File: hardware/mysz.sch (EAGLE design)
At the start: 17 parts, among them IC1 LM1117T(H)-3.3, U1 NUCLEO-L053R8, X2 332-18

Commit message: Add Gyro schemat
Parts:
- removed U$2: DISPLAY-NOKIA-3310, diy-modules:DISPLAY-NOKIA-3310
- removed X2: 332-18, con-garry:332-18
- added GYRO: (no value), pinhead:PINHD-1X10
- added PCD8544: (no value), pinhead:PINHD-1X7/90
- added R3, R4: 22k, rcl:R-EU_0207/10
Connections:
- new net GYRO_CS: GYRO.3
- new net GYRO_DEN: GYRO.1
- new net GYRO_INT1: GYRO.2
- new net GYRO_SCL: GYRO.6, R3.1
- new net GYRO_SDA: GYRO.7, R4.1
- new net LCD_CE: PCD8544.2
- new net LCD_DC: PCD8544.3
- new net LCD_RST: PCD8544.1
- new net N$4: GYRO.10, GYRO.4
- net +3V3: now also R3.2, R4.2
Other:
- moved on the sheet: C1, C2, C3, C4, IC1, POWER

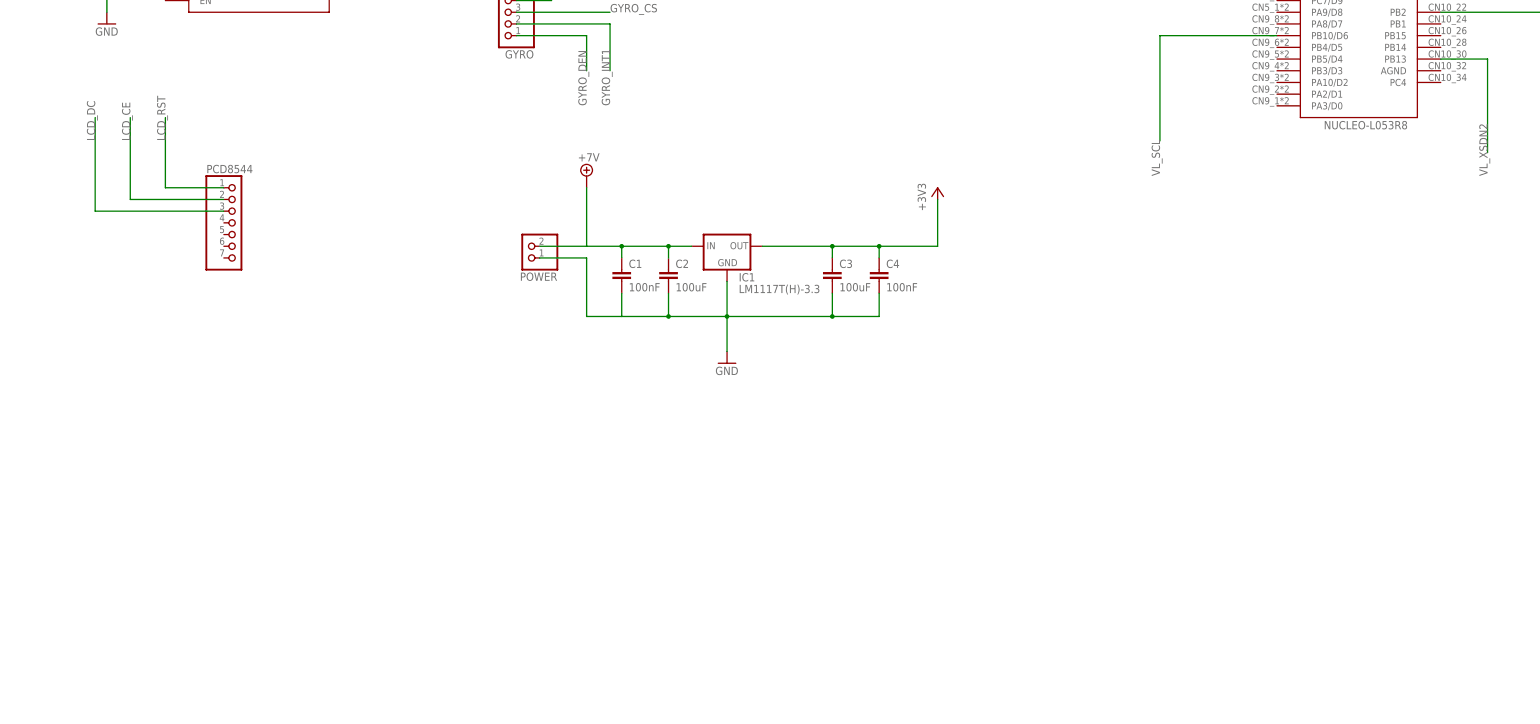
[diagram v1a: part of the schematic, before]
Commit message: Add driver
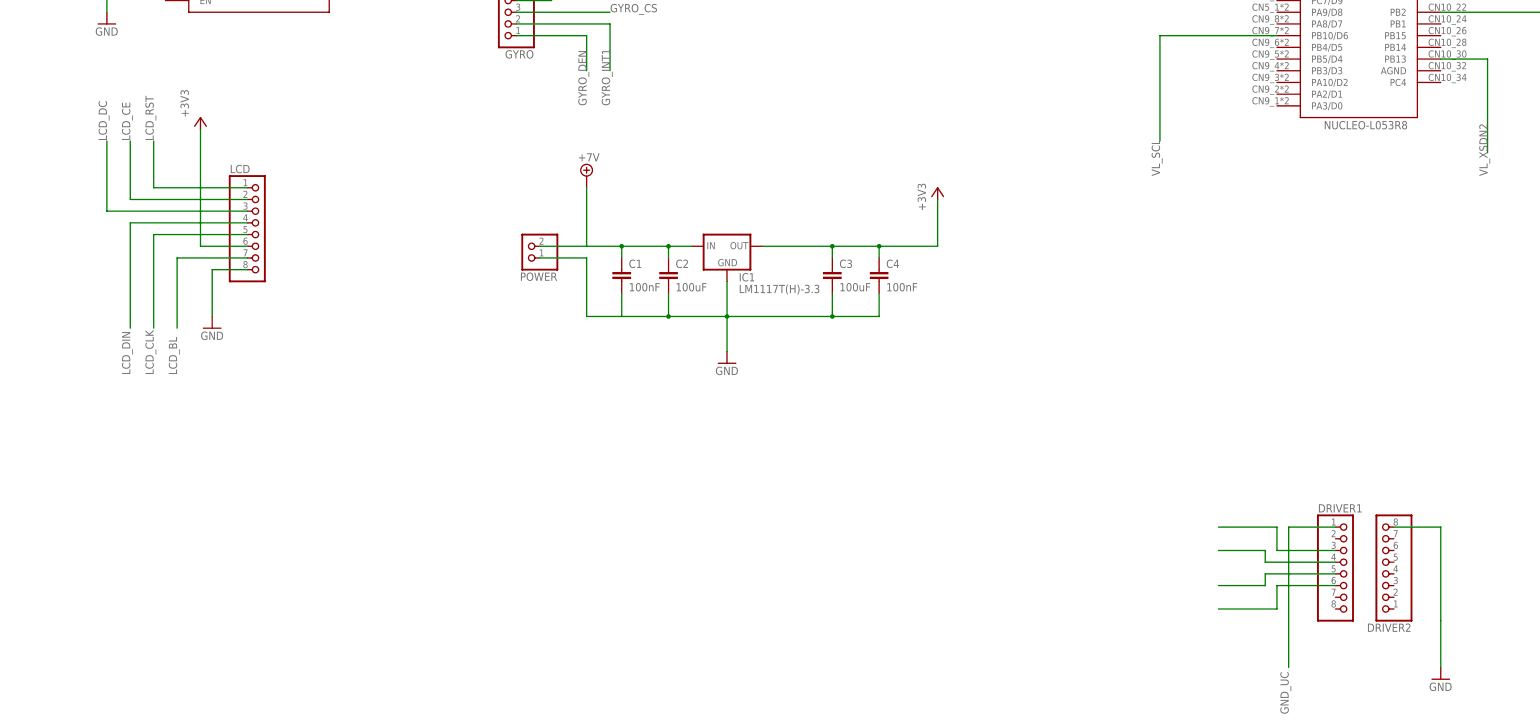
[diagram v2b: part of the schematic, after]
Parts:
- removed PCD8544: (no value), pinhead:PINHD-1X7/90
- added DRIVER1, DRIVER2, LCD: (no value), pinhead:PINHD-1X8
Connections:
- new net GND_UC: DRIVER1.1
- new net LCD_BL: LCD.7
- new net LCD_CLK: LCD.5
- new net LCD_DIN: LCD.4
- new net N$1: DRIVER1.3
- new net N$2: DRIVER1.4
- new net N$3: DRIVER1.5
- new net N$5: DRIVER1.6
- net +3V3: now also LCD.6
- net GND: now also DRIVER2.8, LCD.8
- net LCD_CE: now also LCD.2; no longer PCD8544.2
- net LCD_DC: now also LCD.3; no longer PCD8544.3
- net LCD_RST: now also LCD.1; no longer PCD8544.1
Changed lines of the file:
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@@
 <part name="+3V8" library="supply1" library_urn="urn:adsk.eagle:library:371" deviceset="+3V3" device=""/>
 <part name="GYRO" library="pinhead" library_urn="urn:adsk.eagle:library:325" deviceset="PINHD-1X10" device="" package3d_urn="urn:adsk.eagle:package:22406/2"/>
-<part name="PCD8544" library="pinhead" library_urn="urn:adsk.eagle:library:325" deviceset="PINHD-1X7" device="/90" package3d_urn="urn:adsk.eagle:package:22476/2"/>
+<part name="LCD" library="pinhead" library_urn="urn:adsk.eagle:library:325" deviceset="PINHD-1X8" device="" package3d_urn="urn:adsk.eagle:package:22409/2"/>
+<part name="+3V9" library="supply1" library_urn="urn:adsk.eagle:library:371" deviceset="+3V3" device=""/>
+<part name="GND8" library="supply1" library_urn="urn:adsk.eagle:library:371" deviceset="GND" device=""/>
+<part name="DRIVER1" library="pinhead" library_urn="urn:adsk.eagle:library:325" deviceset="PINHD-1X8" device="" package3d_urn="urn:adsk.eagle:package:22409/2"/>
+<part name="DRIVER2" library="pinhead" library_urn="urn:adsk.eagle:library:325" deviceset="PINHD-1X8" device="" package3d_urn="urn:adsk.eagle:package:22409/2"/>
+<part name="GND9" library="supply1" library_urn="urn:adsk.eagle:library:371" deviceset="GND" device=""/>
 </parts>
 <sheets>
@@
 <attribute name="VALUE" x="107.95" y="35.56" size="1.778" layer="96" rot="R180"/>
 </instance>
-<instance part="PCD8544" gate="A" x="43.18" y="-33.02" smashed="yes">
-<attribute name="NAME" x="36.83" y="-22.225" size="1.778" layer="95"/>
-<attribute name="VALUE" x="36.83" y="-45.72" size="1.778" layer="96"/>
+<instance part="LCD" gate="A" x="48.26" y="-35.56" smashed="yes">
+<attribute name="NAME" x="41.91" y="-22.225" size="1.778" layer="95"/>
+<attribute name="VALUE" x="41.91" y="-48.26" size="1.778" layer="96"/>
+</instance>
+<instance part="+3V9" gate="G$1" x="35.56" y="-10.16" smashed="yes">
+<attribute name="VALUE" x="33.02" y="-10.16" size="1.778" layer="96" rot="R90"/>
+</instance>
+<instance part="GND8" gate="1" x="38.1" y="-55.88" smashed="yes">
+<attribute name="VALUE" x="35.56" y="-58.42" size="1.778" layer="96"/>
+</instance>
+<instance part="DRIVER1" gate="A" x="284.48" y="-109.22" smashed="yes">
+<attribute name="NAME" x="278.13" y="-95.885" size="1.778" layer="95"/>
+<attribute name="VALUE" x="278.13" y="-121.92" size="1.778" layer="96"/>
+</instance>
+<instance part="DRIVER2" gate="A" x="292.1" y="-106.68" smashed="yes" rot="R180">
+<attribute name="NAME" x="298.45" y="-120.015" size="1.778" layer="95" rot="R180"/>
+<attribute name="VALUE" x="298.45" y="-93.98" size="1.778" layer="96" rot="R180"/>
+</instance>
+<instance part="GND9" gate="1" x="304.8" y="-132.08" smashed="yes">
+<attribute name="VALUE" x="302.26" y="-134.62" size="1.778" layer="96"/>
 </instance>
 </instances>
@@
 <pinref part="GND7" gate="1" pin="GND"/>
 </segment>
+<segment>
+<pinref part="LCD" gate="A" pin="8"/>
+<wire x1="45.72" y1="-43.18" x2="38.1" y2="-43.18" width="0.1524" layer="91"/>
+<wire x1="38.1" y1="-43.18" x2="38.1" y2="-53.34" width="0.1524" layer="91"/>
+<pinref part="GND8" gate="1" pin="GND"/>
+</segment>
+<segment>
+<pinref part="DRIVER2" gate="A" pin="8"/>
+<wire x1="294.64" y1="-99.06" x2="304.8" y2="-99.06" width="0.1524" layer="91"/>
+<wire x1="304.8" y1="-99.06" x2="304.8" y2="-119.38" width="0.1524" layer="91"/>
+<wire x1="304.8" y1="-119.38" x2="304.8" y2="-129.54" width="0.1524" layer="91"/>
+<pinref part="GND9" gate="1" pin="GND"/>
+</segment>
 </net>
 <net name="BT_TX" class="0">
@@
 <pinref part="+3V8" gate="G$1" pin="+3V3"/>
 </segment>
+<segment>
+<pinref part="LCD" gate="A" pin="6"/>
+<wire x1="45.72" y1="-38.1" x2="35.56" y2="-38.1" width="0.1524" layer="91"/>
+<wire x1="35.56" y1="-38.1" x2="35.56" y2="-12.7" width="0.1524" layer="91"/>
+<pinref part="+3V9" gate="G$1" pin="+3V3"/>
+</segment>
 </net>
 <net name="ENC_L_B" class="0">
@@
 <net name="LCD_RST" class="0">
 <segment>
-<pinref part="PCD8544" gate="A" pin="1"/>
-<wire x1="40.64" y1="-25.4" x2="27.94" y2="-25.4" width="0.1524" layer="91"/>
-<label x="27.94" y="-15.24" size="1.778" layer="95" rot="R90"/>
-<wire x1="27.94" y1="-25.4" x2="27.94" y2="-10.16" width="0.1524" layer="91"/>
+<label x="25.4" y="-15.24" size="1.778" layer="95" rot="R90"/>
+<wire x1="25.4" y1="-25.4" x2="25.4" y2="-15.24" width="0.1524" layer="91"/>
+<pinref part="LCD" gate="A" pin="1"/>
+<wire x1="45.72" y1="-25.4" x2="25.4" y2="-25.4" width="0.1524" layer="91"/>
 </segment>
 </net>
 <net name="LCD_CE" class="0">
 <segment>
-<pinref part="PCD8544" gate="A" pin="2"/>
-<wire x1="40.64" y1="-27.94" x2="20.32" y2="-27.94" width="0.1524" layer="91"/>
-<wire x1="20.32" y1="-27.94" x2="20.32" y2="-10.16" width="0.1524" layer="91"/>
+<wire x1="20.32" y1="-27.94" x2="20.32" y2="-15.24" width="0.1524" layer="91"/>
 <label x="20.32" y="-15.24" size="1.778" layer="95" rot="R90"/>
+<pinref part="LCD" gate="A" pin="2"/>
+<wire x1="45.72" y1="-27.94" x2="20.32" y2="-27.94" width="0.1524" layer="91"/>
 </segment>
 </net>
 <net name="LCD_DC" class="0">
 <segment>
-<pinref part="PCD8544" gate="A" pin="3"/>
-<wire x1="40.64" y1="-30.48" x2="12.7" y2="-30.48" width="0.1524" layer="91"/>
-<wire x1="12.7" y1="-30.48" x2="12.7" y2="-10.16" width="0.1524" layer="91"/>
-<label x="12.7" y="-15.24" size="1.778" layer="95" rot="R90"/>
-</segment>
-</net>
+<wire x1="15.24" y1="-30.48" x2="15.24" y2="-15.24" width="0.1524" layer="91"/>
+<label x="15.24" y="-15.24" size="1.778" layer="95" rot="R90"/>
+<pinref part="LCD" gate="A" pin="3"/>
+<wire x1="45.72" y1="-30.48" x2="15.24" y2="-30.48" width="0.1524" layer="91"/>
+</segment>
+</net>
+<net name="LCD_DIN" class="0">
+<segment>
+<wire x1="20.32" y1="-33.02" x2="20.32" y2="-55.88" width="0.1524" layer="91"/>
+<label x="20.32" y="-66.04" size="1.778" layer="95" rot="R90"/>
+<pinref part="LCD" gate="A" pin="4"/>
+<wire x1="45.72" y1="-33.02" x2="20.32" y2="-33.02" width="0.1524" layer="91"/>
+</segment>
+</net>
+<net name="LCD_CLK" class="0">
+<segment>
+<wire x1="25.4" y1="-35.56" x2="25.4" y2="-55.88" width="0.1524" layer="91"/>
+<label x="25.4" y="-66.04" size="1.778" layer="95" rot="R90"/>
+<pinref part="LCD" gate="A" pin="5"/>
+<wire x1="45.72" y1="-35.56" x2="25.4" y2="-35.56" width="0.1524" layer="91"/>
+</segment>
+</net>
+<net name="LCD_BL" class="0">
+<segment>
+<pinref part="LCD" gate="A" pin="7"/>
+<wire x1="45.72" y1="-40.64" x2="30.48" y2="-40.64" width="0.1524" layer="91"/>
+<wire x1="30.48" y1="-40.64" x2="30.48" y2="-55.88" width="0.1524" layer="91"/>
+<label x="30.48" y="-66.04" size="1.778" layer="95" rot="R90"/>
+</segment>
+</net>
+<net name="GND_UC" class="0">
+<segment>
+<pinref part="DRIVER1" gate="A" pin="1"/>
+<wire x1="281.94" y1="-99.06" x2="271.78" y2="-99.06" width="0.1524" layer="91"/>
+<wire x1="271.78" y1="-99.06" x2="271.78" y2="-129.54" width="0.1524" layer="91"/>
+<label x="271.78" y="-139.7" size="1.778" layer="95" rot="R90"/>
+</segment>
+</net>
+<net name="N$2" class="0">
+<segment>
+<pinref part="DRIVER1" gate="A" pin="4"/>
+<wire x1="281.94" y1="-106.68" x2="266.7" y2="-106.68" width="0.1524" layer="91"/>
+<wire x1="266.7" y1="-106.68" x2="266.7" y2="-104.14" width="0.1524" layer="91"/>
+<wire x1="266.7" y1="-104.14" x2="256.54" y2="-104.14" width="0.1524" layer="91"/>
+</segment>
+</net>
+<net name="N$3" class="0">
+<segment>
+<pinref part="DRIVER1" gate="A" pin="5"/>
+<wire x1="281.94" y1="-109.22" x2="266.7" y2="-109.22" width="0.1524" layer="91"/>
+<wire x1="266.7" y1="-109.22" x2="266.7" y2="-111.76" width="0.1524" layer="91"/>
+<wire x1="266.7" y1="-111.76" x2="256.54" y2="-111.76" width="0.1524" layer="91"/>
+</segment>
+</net>
+<net name="N$5" class="0">
+<segment>
+<pinref part="DRIVER1" gate="A" pin="6"/>
+<wire x1="281.94" y1="-111.76" x2="269.24" y2="-111.76" width="0.1524" layer="91"/>
+<wire x1="269.24" y1="-111.76" x2="269.24" y2="-116.84" width="0.1524" layer="91"/>
+<wire x1="269.24" y1="-116.84" x2="256.54" y2="-116.84" width="0.1524" layer="91"/>
+</segment>
+</net>
+<net name="N$1" class="0">
+<segment>
+<pinref part="DRIVER1" gate="A" pin="3"/>
+<wire x1="281.94" y1="-104.14" x2="269.24" y2="-104.14" width="0.1524" layer="91"/>
+<wire x1="269.24" y1="-104.14" x2="269.24" y2="-99.06" width="0.1524" layer="91"/>
+<wire x1="269.24" y1="-99.06" x2="256.54" y2="-99.06" width="0.1524" layer="91"/>
+</segment>
+</net>
